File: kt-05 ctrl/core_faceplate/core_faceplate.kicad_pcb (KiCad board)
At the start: 2 copper layers, 50.8 x 76.2 mm, 15 parts, among them CN1 YTC1P-6030-01, CN15 YTC1P-6030-01, CN16 YTC1P-6030-01, CN17 YTC1P-6030-01, CN18 YTC1P-6030-01, CN19 YTC1P-6030-01, CN2 YTC1P-6030-01, CN20 YTC1P-6030-01, CN21 YTC1P-6030-01, CN22 YTC1P-6030-01, CN4 YTC1P-6030-01

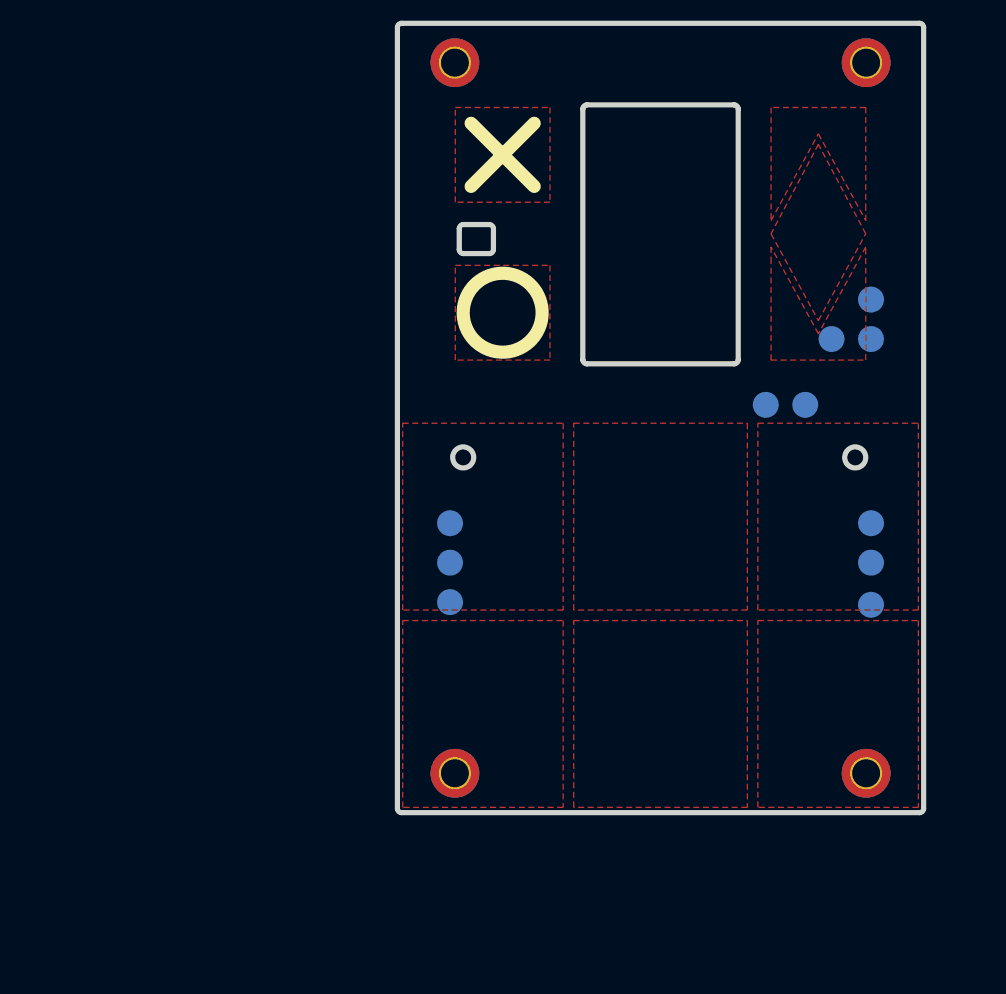
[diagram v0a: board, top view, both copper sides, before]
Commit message: improved fuses
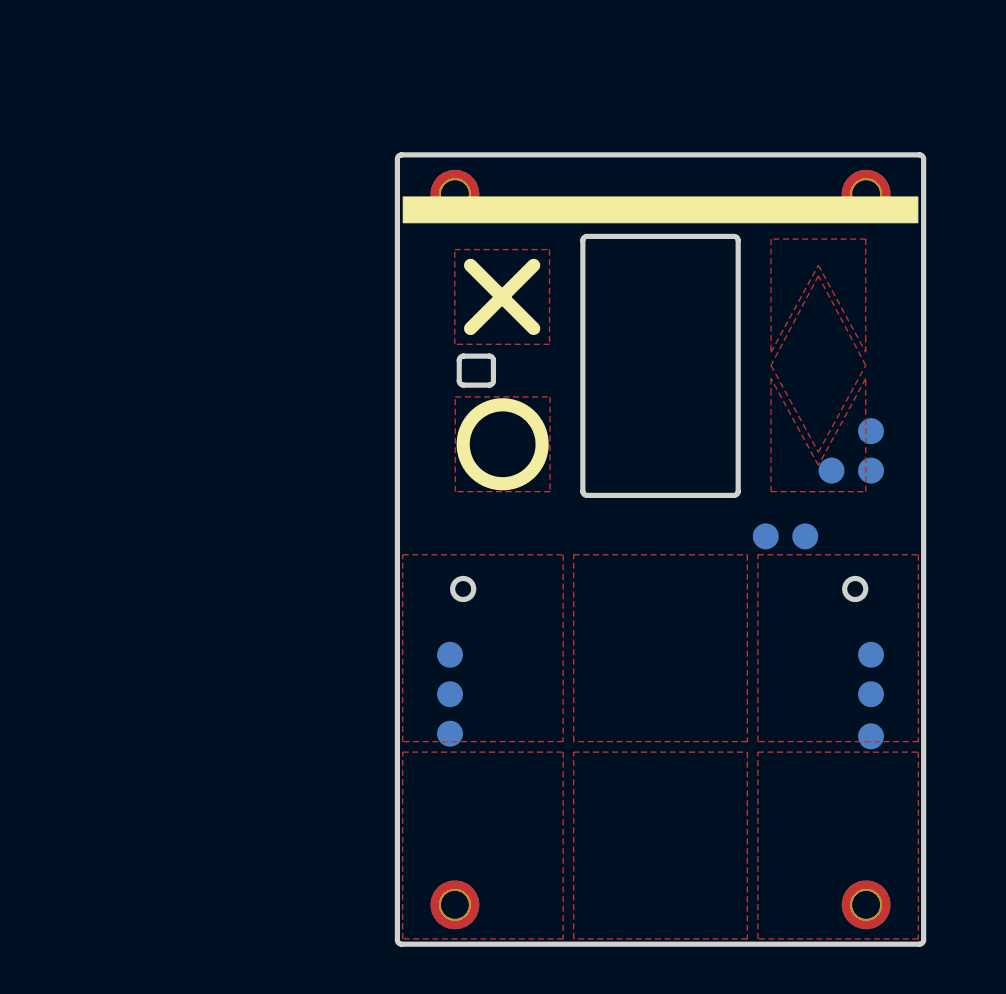
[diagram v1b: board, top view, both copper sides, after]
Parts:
- moved CN15 12.7 mm to (121.9, 55.9)
- moved CN16 12.7 mm to (118.1, 55.9)
- moved CN18 12.7 mm to (121.9, 77.5)
- moved CN19 12.7 mm to (121.9, 81.5)
- moved CN20 12.7 mm to (81.3, 81.3)
- moved CN21 12.7 mm to (81.3, 77.5)
- moved CN4 12.7 mm to (121.9, 52.1)
- moved H3 12.7 mm to (121.5, 97.8)
- moved H4 12.7 mm to (81.8, 97.8)
- moved H1 12.7 mm to (81.8, 29.2)
- moved H2 12.7 mm to (121.5, 29.2)
- moved CN1 12.7 mm to (111.8, 62.2)
- moved CN17 12.7 mm to (121.9, 73.7)
- moved CN2 12.7 mm to (115.6, 62.2)
- moved CN22 12.7 mm to (81.3, 73.7)

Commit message: n
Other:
- board text added: "CAPACITIVE TOUCH PADS"
- board text added: "ESP BOOT0"
- board text added: "ESP RESET"
- board text added: "MIDI IN"
- board text added: "MIDI OUT"
- board text added: "SYSTEM POWER"
- board text added: "TT0.1"
- board text added: "TWO-WIRE INTERFACE 0"
- board text added: "TWO-WIRE INTERFACE 1"
- board text added: "TYPE-C"

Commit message: n
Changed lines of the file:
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@@
 		)
+	)
+	(gr_poly
+		(pts
+			(xy 121.9708 33.5788) (xy 121.9708 40.513) (xy 122.555 40.513) (xy 122.555 50.927) (xy 121.9708 50.927)
+			(xy 121.9708 57.8612) (xy 126.4412 57.8612) (xy 126.4412 33.5788)
+		)
+		(stroke
+			(width 0.1)
+			(type solid)
+		)
+		(fill yes)
+		(layer "F.Cu")
+	)
+	(gr_rect
+		(start 76.7588 34.5948)
+		(end 81.2292 57.8612)
+		(stroke
+			(width 0.1)
+			(type solid)
+		)
+		(fill yes)
+		(layer "F.Cu")
 	)
 	(gr_rect
@@
 	)
 	(gr_rect
+		(start 121.539 40.64)
+		(end 122.428 50.8)
+		(stroke
+			(width 0.1)
+			(type solid)
+		)
+		(fill yes)
+		(layer "F.Mask")
+	)
+	(gr_rect
 		(start 91.44 54.4068)
 		(end 92.9132 54.8132)
@@
 		(layer "F.Mask")
 	)
+	(gr_rect
+		(start 121.539 40.64)
+		(end 122.428 50.8)
+		(stroke
+			(width 0.1)
+			(type solid)
+		)
+		(fill yes)
+		(layer "B.Mask")
+	)
 	(gr_poly

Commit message: hall faceplate
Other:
- board text added: "0"
- board text added: "1"
- board text added: "2"
- board text added: "3"
- board text added: "4"
- board text added: "5"
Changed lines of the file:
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@@
+		)
+	)
+	(gr_text "3"
+		(at 76.708 100.838 0)
+		(layer "F.SilkS" knockout)
+		(effects
+			(font
+				(size 1.5 1.5)
+				(thickness 0.3)
+				(bold yes)
+			)
+			(justify left bottom)
 		)
 	)
@@
 		)
 	)
+	(gr_text "1"
+		(at 108.204 81.788 0)
+		(layer "F.SilkS" knockout)
+		(effects
+			(font
+				(size 1.5 1.5)
+				(thickness 0.3)
+				(bold yes)
+			)
+			(justify left bottom)
+		)
+	)
+	(gr_text "5"
+		(at 110.998 100.838 0)
+		(layer "F.SilkS" knockout)
+		(effects
+			(font
+				(size 1.5 1.5)
+				(thickness 0.3)
+				(bold yes)
+			)
+			(justify left bottom)
+		)
+	)
 	(gr_text "TWO-WIRE INTERFACE 0"
 		(at 114.808 60.96 0)
@@
 			)
 			(justify bottom)
+		)
+	)
+	(gr_text "2"
+		(at 124.714 81.788 0)
+		(layer "F.SilkS" knockout)
+		(effects
+			(font
+				(size 1.5 1.5)
+				(thickness 0.3)
+				(bold yes)
+			)
+			(justify left bottom)
 		)
 	)
@@
 		)
 	)
+	(gr_text "0"
+		(at 90.424 81.788 0)
+		(layer "F.SilkS" knockout)
+		(effects
+			(font
+				(size 1.5 1.5)
+				(thickness 0.3)
+				(bold yes)
+			)
+			(justify left bottom)
+		)
+	)
+	(gr_text "4"
+		(at 93.218 100.838 0)
+		(layer "F.SilkS" knockout)
+		(effects
+			(font
+				(size 1.5 1.5)
+				(thickness 0.3)
+				(bold yes)
+			)
+			(justify left bottom)
+		)
+	)

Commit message: q
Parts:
- added G***: LOGO, LOGO, F.Cu at (79.2, 48.8)
- added G***: LOGO, LOGO, F.Cu at (124.2, 54.9)
- added G***: LOGO, LOGO, F.Cu at (125.7, 43.6)
- added G***: LOGO, LOGO, F.Cu at (62.6, 52.3)
- added G***: LOGO, LOGO, F.Cu at (125.8, 51.0)
- added G***: LOGO, LOGO, F.Cu at (128.3, 55.9)
- added G***: LOGO, LOGO, F.Cu at (46.2, 49.8)
- added G***: LOGO, LOGO, F.Cu at (42.4, 60.5)
- added G***: LOGO, LOGO, F.Cu at (75.2, 55.6)
- added G***: LOGO, LOGO, F.Cu at (76.2, 51.1)
- added G***: LOGO, LOGO, F.Cu at (46.5, 39.6)
- added G***: LOGO, LOGO, F.Cu at (128.8, 32.3)
- added G***: LOGO, LOGO, F.Cu at (126.0, 46.7)
- added G***: LOGO, LOGO, F.Cu at (63.7, 38.0)
- added G***: LOGO, LOGO, F.Cu at (63.6, 48.1)
- added G***: LOGO, LOGO, F.Cu at (63.6, 58.0)
- added G***: LOGO, LOGO, F.Cu at (62.6, 42.1)
- added G***: LOGO, LOGO, F.Cu at (124.2, 35.3)
- added G***: LOGO, LOGO, F.Cu at (75.9, 45.0)
- added G***: LOGO, LOGO, F.Cu at (48.3, 44.2)
- added G***: LOGO, LOGO, F.Cu at (42.4, 50.5)
- added G***: LOGO, LOGO, F.Cu at (50.3, 48.8)
- added G***: LOGO, LOGO, F.Cu at (48.0, 54.4)
- added G***: LOGO, LOGO, F.Cu at (50.0, 38.6)
- added G***: LOGO, LOGO, F.Cu at (42.7, 40.1)
- added G***: LOGO, LOGO, F.Cu at (75.7, 39.1)
- added G***: LOGO, LOGO, F.Cu at (44.2, 45.2)
- added G***: LOGO, LOGO, F.Cu at (79.2, 42.9)
- added G***: LOGO, LOGO, F.Cu at (79.2, 54.9)
- added G***: LOGO, LOGO, F.Cu at (44.2, 55.4)
- added G***: LOGO, LOGO, F.Cu at (75.2, 33.5)
- added G***: LOGO, LOGO, F.Cu at (125.4, 39.4)
- added G***: LOGO, LOGO, F.Cu at (79.2, 37.1)

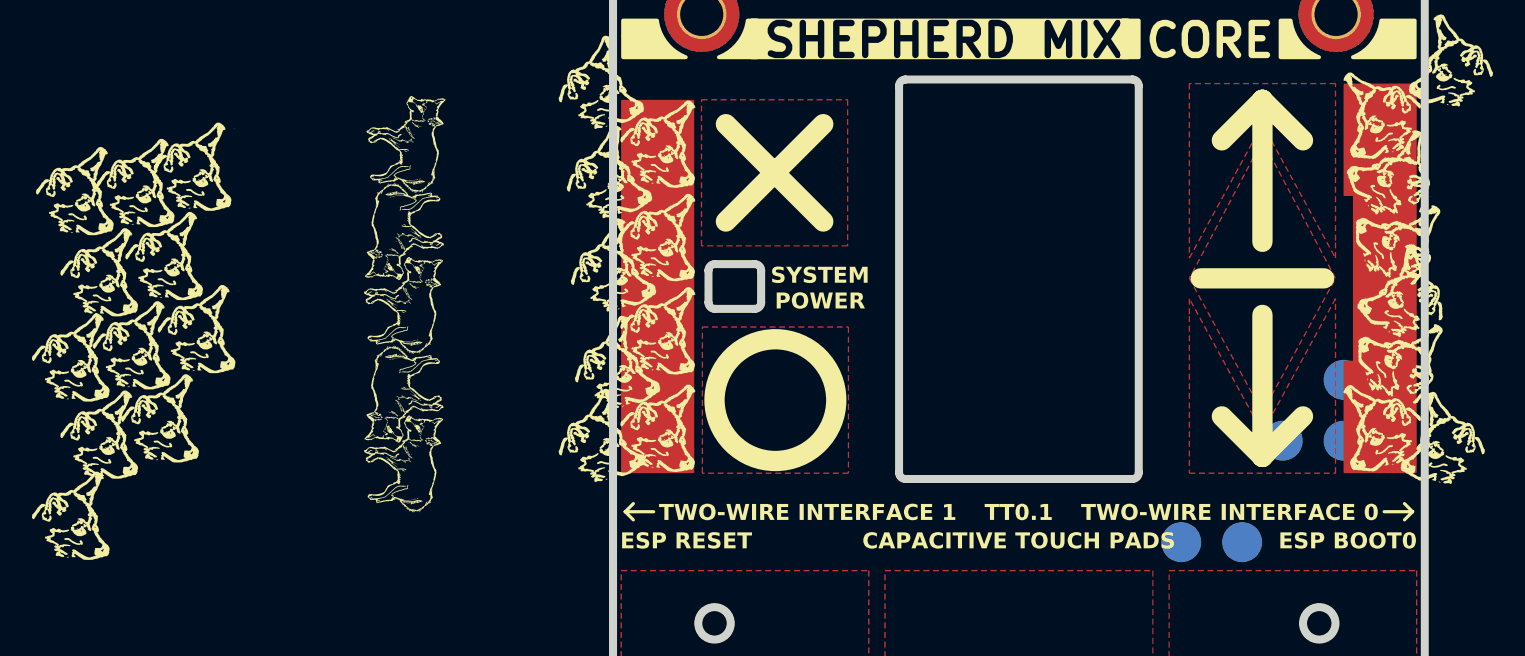
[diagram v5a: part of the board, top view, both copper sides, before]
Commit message: faceplate designs
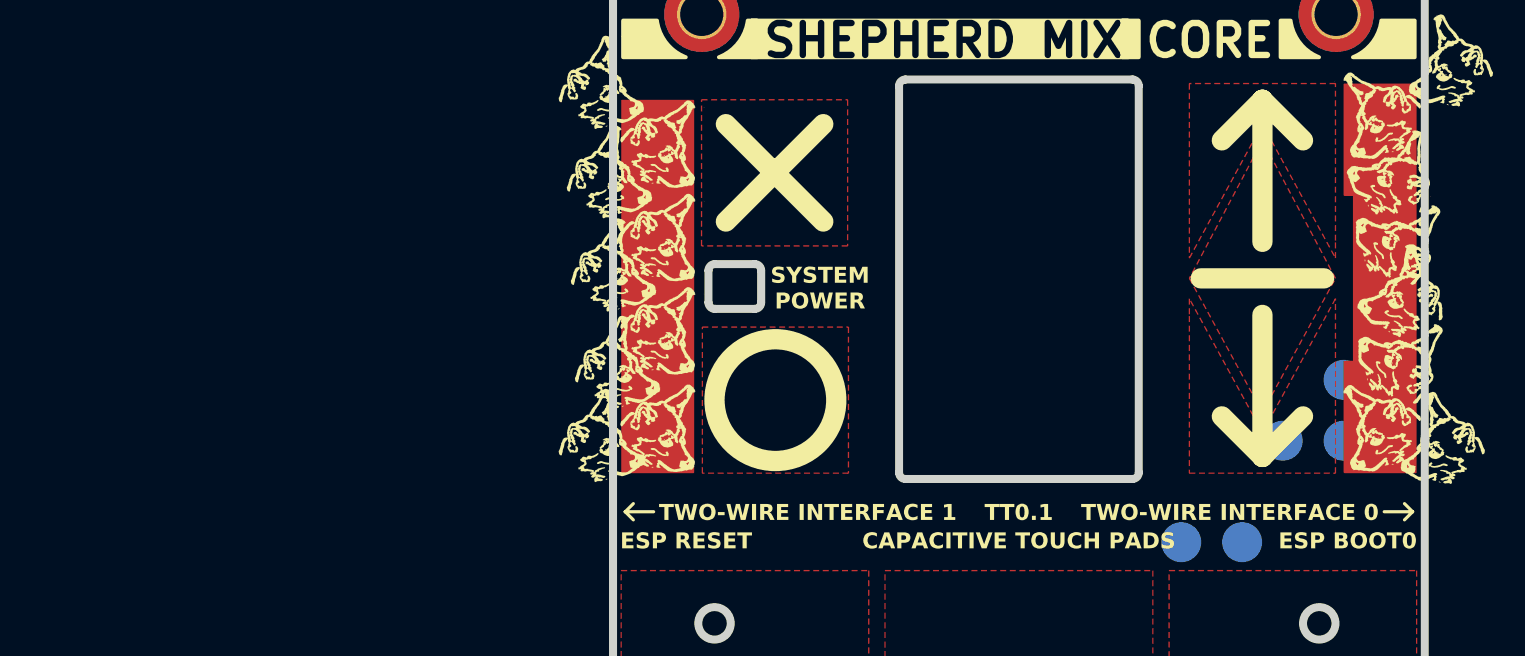
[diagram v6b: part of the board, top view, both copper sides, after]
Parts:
- removed the G*** at (62.6, 52.3)
- removed the G*** at (46.2, 49.8)
- removed the G*** at (42.4, 60.5)
- removed the G*** at (46.5, 39.6)
- removed the G*** at (63.7, 38.0)
- removed the G*** at (63.6, 48.1)
- removed the G*** at (63.6, 58.0)
- removed the G*** at (62.6, 42.1)
- removed the G*** at (48.3, 44.2)
- removed the G*** at (42.4, 50.5)
- removed the G*** at (50.3, 48.8)
- removed the G*** at (48.0, 54.4)
- removed the G*** at (50.0, 38.6)
- removed the G*** at (42.7, 40.1)
- removed the G*** at (44.2, 45.2)
- removed the G*** at (44.2, 55.4)

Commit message: production 1
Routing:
- added copper zone on B.Cu, net (none)
